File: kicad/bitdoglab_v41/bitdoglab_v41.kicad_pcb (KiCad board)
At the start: 2 copper layers, 87.9 x 123.9 mm, 58 parts, among them J1 Conn_01x20_Socket, J10 3V3, J100 JST_EH_B4B-EH-A_1x04_P2.50mm_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, J101 JST_EH_B4B-EH-A_1x04_P2.50mm_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, J11 5V-VBUS, J12 Conn_01x05_Pin, J13 Conn_01x05_Pin, J14 5x5 Matrix led, J15 0, J16 1, J17 2, J18 3, J19 JOYSTICK, J2 conector_idc, J3 Conn_01x20_Socket, J4 jumper_mic, J5 Conn_01x05_Pin, J6 Conn_01x05_Pin, J7 GND, J8 ANA-IN, J9 GND, Q1 DMG2305UX-13, Q2 BC337, Q3 BC337, SW1 Reset, SW2 Botão, SW3 Button_B, U1 3.3v_tht, U4 MIC

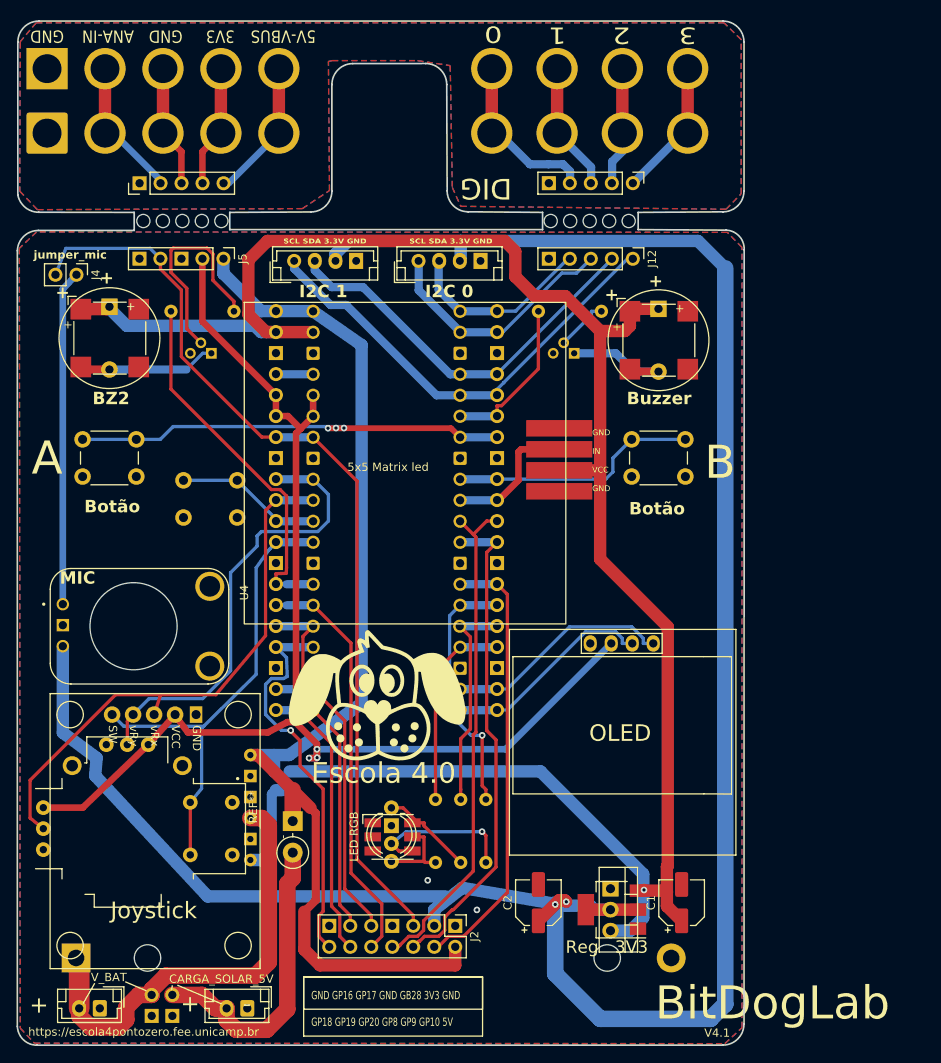
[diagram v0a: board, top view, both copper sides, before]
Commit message: Mudar VBUS para VSYS no IDC e JACARE
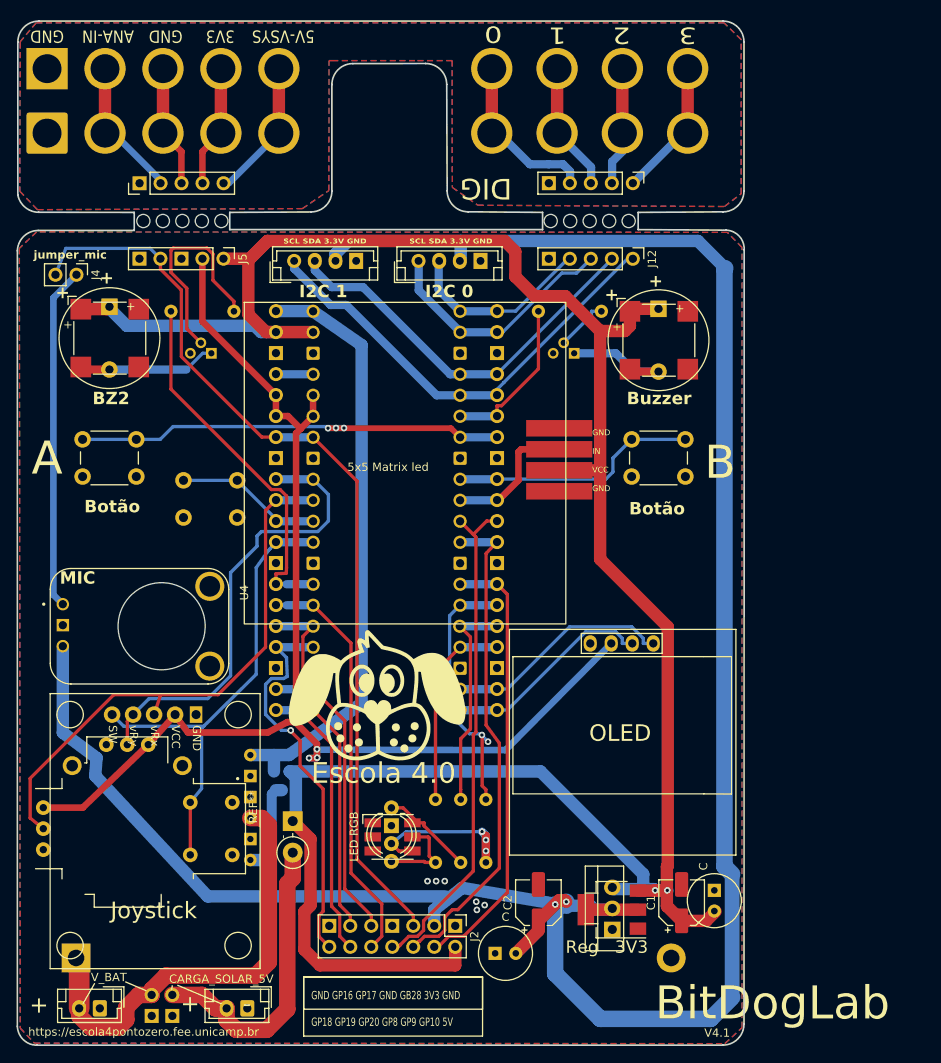
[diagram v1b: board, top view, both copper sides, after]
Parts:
- added C: C_Radial_D6.3mm_H7.0mm_P2.50mm, Capacitor_THT:C_Radial_D6.3mm_H7.0mm_P2.50mm, F.Cu at (145.9, 145.0)
- added C: C_Radial_D6.3mm_H7.0mm_P2.50mm, Capacitor_THT:C_Radial_D6.3mm_H7.0mm_P2.50mm, F.Cu at (172.4, 137.4)
- J11: value 5V-VBUS -> 5V-VSYS
- moved U1 4.93 mm to (160.1, 142.1), turned to 90 degrees
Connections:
- net VBUS_EXT renamed /VSYS_EXT
- Diode Shottky pad 1: VBUS -> VSYS
- J2 pad 2: VBUS -> VSYS
- J5 pad 1: VBUS -> VSYS
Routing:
- net VBUS: track 135.5 -> 72.4 mm
- net VSYS: track 241.5 -> 295.4 mm, vias 1 -> 2
- net +3.3V: track 275.7 -> 281.6 mm
- net Net-(D1-BA): track 18.3 -> 22.2 mm, vias 1 -> 3
- net /GP11: track 31.1 -> 32.2 mm, vias 1 -> 2
- net Net-(D1-GA): track 9.75 -> 10.7 mm
- net Net-(J4-Pin_1): track 40.5 -> 41.5 mm
- net /pino_31: track 67.9 -> 68.5 mm
- net /GP09: track 59.7 -> 60.3 mm
- net GNDREF: vias 3 -> 7
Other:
- outline, holes or cut-outs redrawn
